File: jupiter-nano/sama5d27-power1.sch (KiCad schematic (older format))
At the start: 1 part, among them U1 ATSAMA5D27C-LD1G-CU

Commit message: WIP – power3 done
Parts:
- removed unit 8 of U1
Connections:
- net labels added: GND, VDDBU, VDDCORE, VDDIODDR, VDDIOP0, VDD_1V2, VDD_1V8
- wire segments 0 -> 128
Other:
- note added: "Power Links"
- moved on the sheet: U1F, U1G, U1I

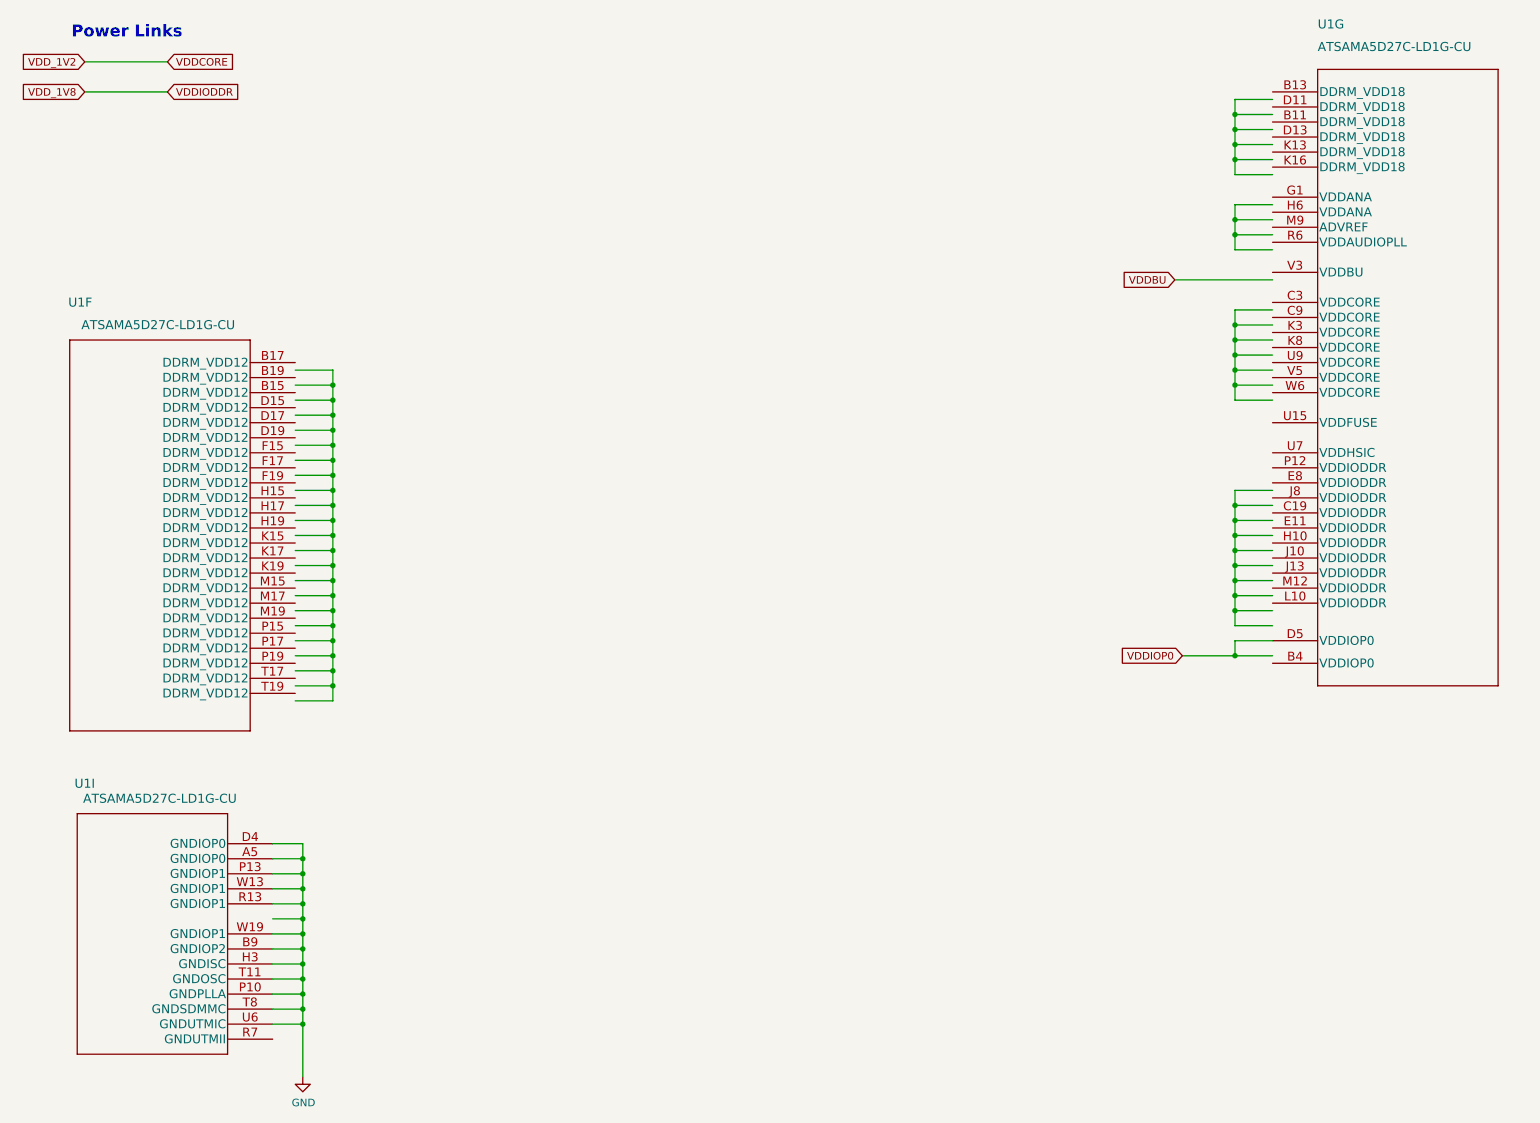
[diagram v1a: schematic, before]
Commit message: added compoent numbers for power
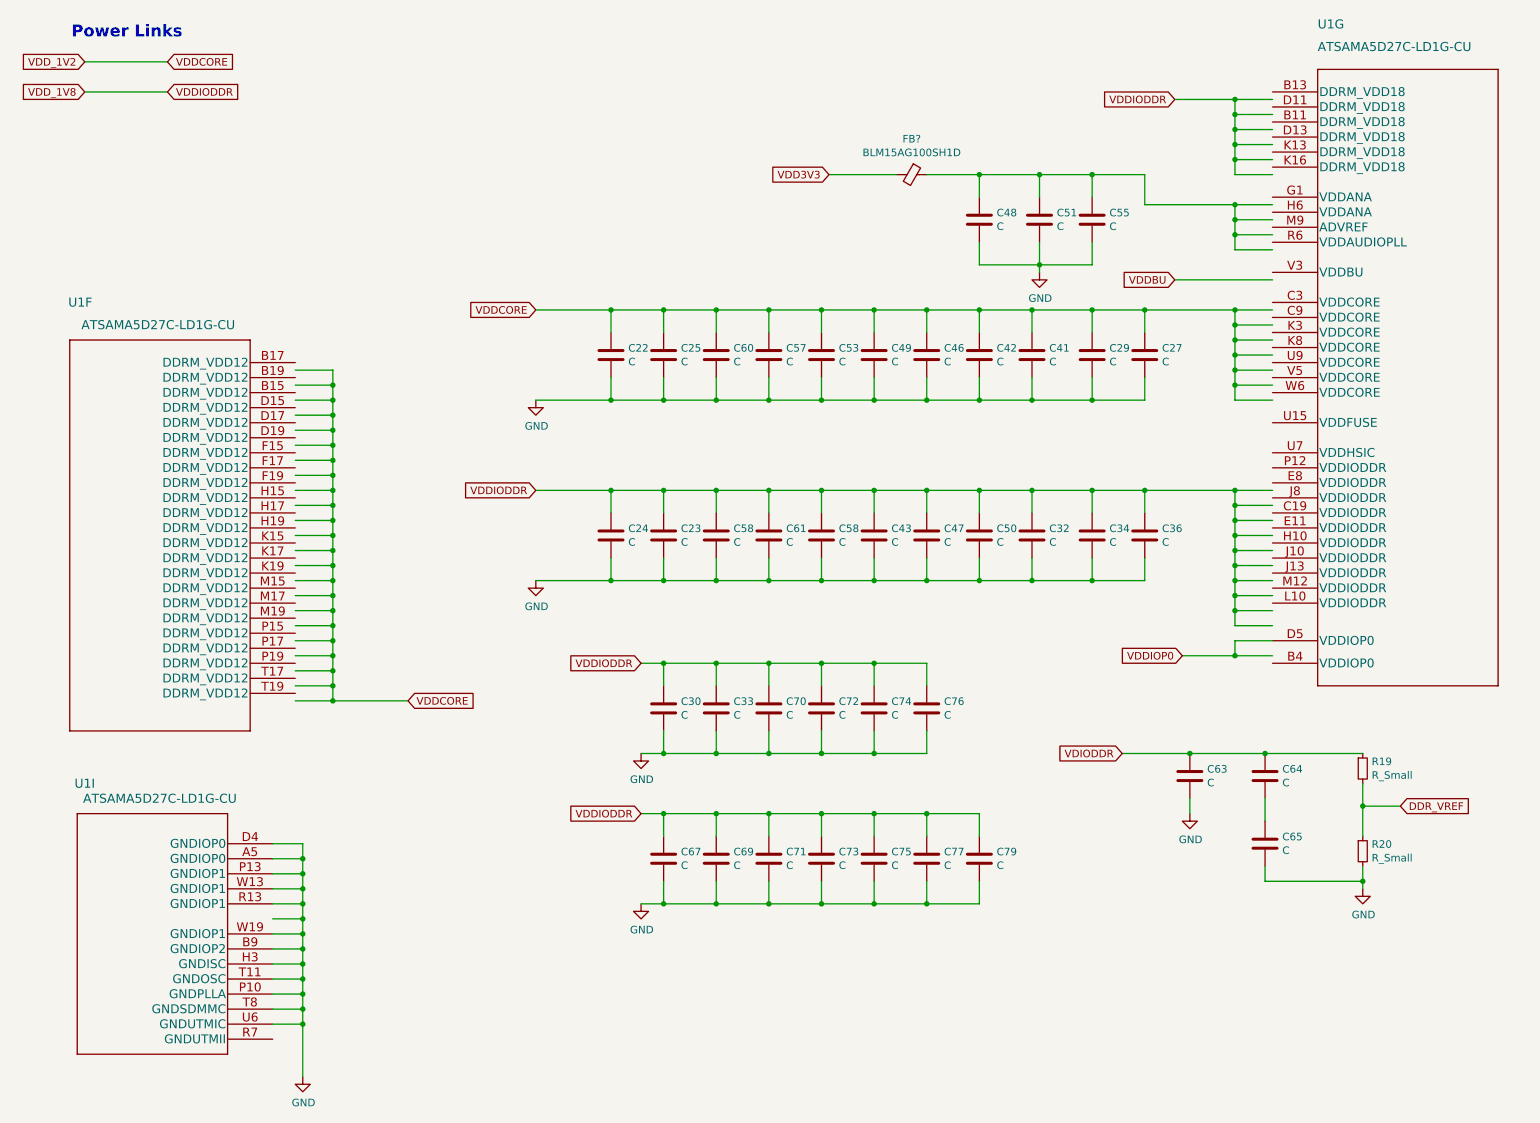
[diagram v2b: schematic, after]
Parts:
- added C22, C23, C24, C25, C27, C29, C30, C32, C33, C34, C36, C41, C42, C43, C46, C47, C48, C49, C50, C51, C53, C55, C57, C58 (x2), C60, C61, C63, C64, C65, C67, C69, C70, C71, C72, C73, C74, C75, C76, C77, C79: C, symbol Device:C
- added FB?: BLM15AG100SH1D, Capacitor_SMD:C_0402_1005Metric, symbol Device:Ferrite_Bead_Small
- added R19, R20: R_Small, symbol Device:R_Small
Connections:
- net labels added: DDR_VREF, VDD3V3, VDIODDR
- wire segments 128 -> 300

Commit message: values for power capacitors
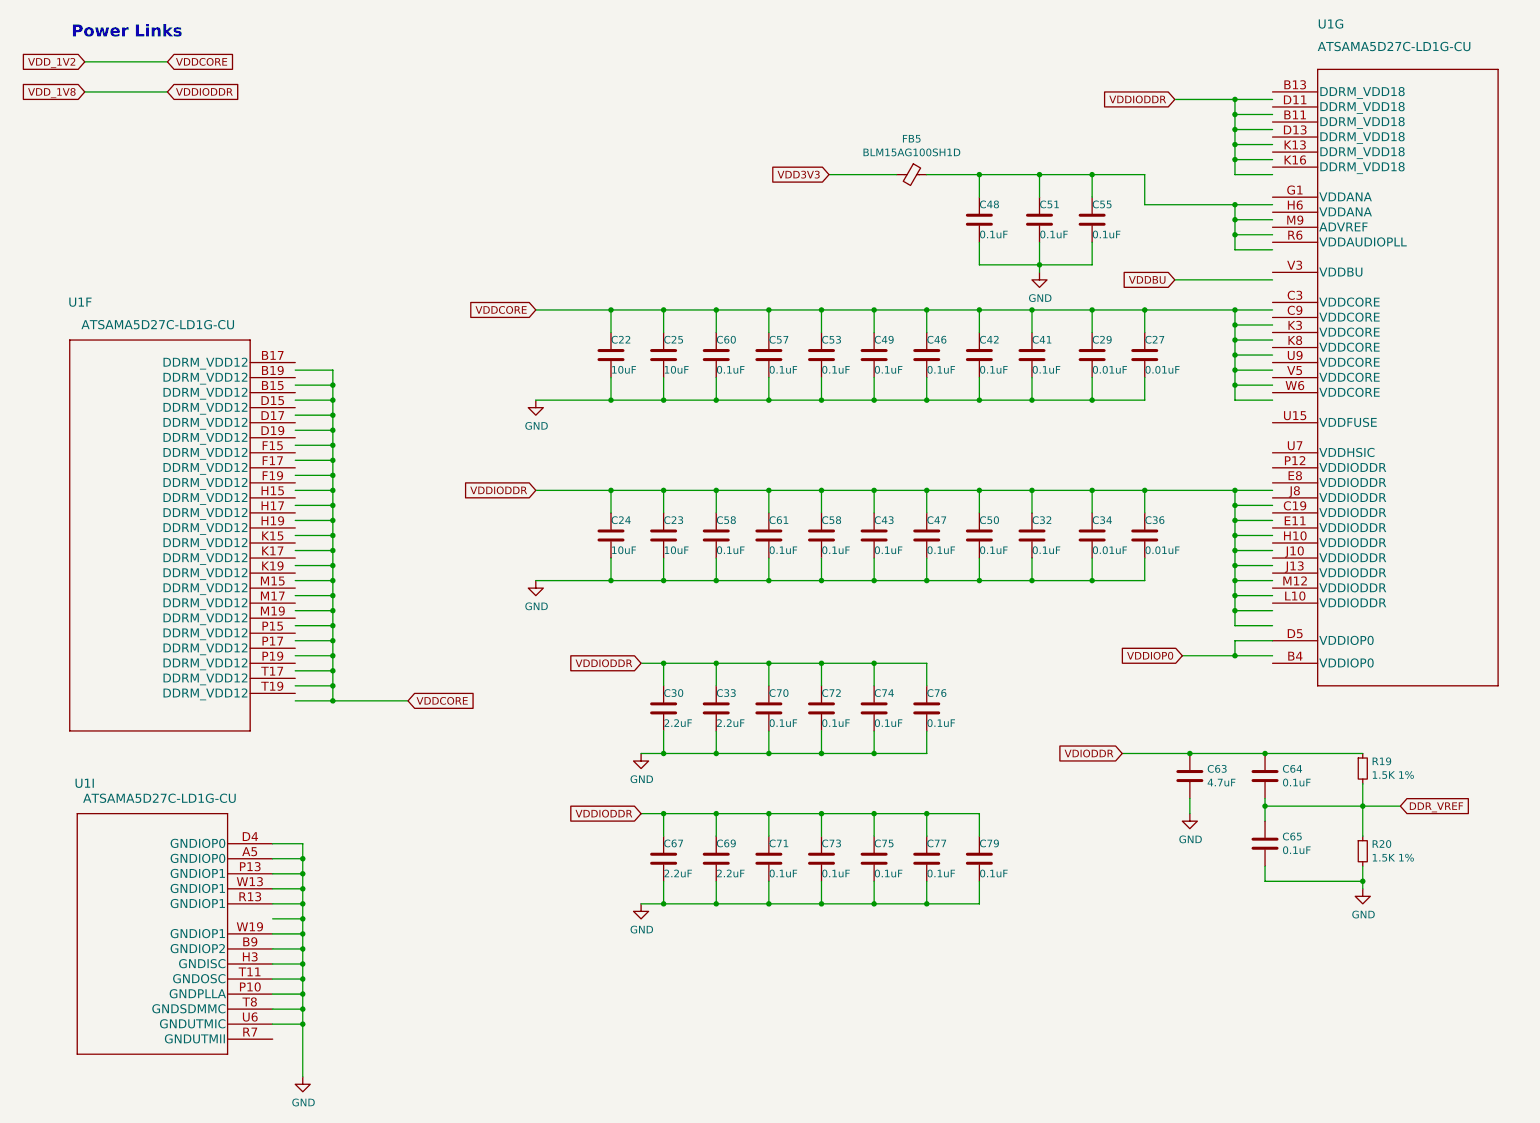
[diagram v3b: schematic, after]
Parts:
- C22, C23, C24, C25: value C -> 10uF
- C27, C29, C34, C36: value C -> 0.01uF
- C30, C33, C67, C69: value C -> 2.2uF
- C32, C41, C42, C43, C46, C47, C48, C49, C50, C51, C53, C55, C57, C58, C60, C61, C64, C65, C70, C71, C72, C73, C74, C75, C76, C77, C79: value C -> 0.1uF
- C63: value C -> 4.7uF
- R19, R20: value R_Small -> 1.5K 1%
- gave numbers to parts that had none: 1
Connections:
- wire segments 300 -> 302

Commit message: WIP, power done
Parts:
- added C40, C59, C62: 0.1uF, symbol Device:C
- added FB?: BLM15AG100SH1D, Capacitor_SMD:C_0402_1005Metric, symbol Device:Ferrite_Bead_Small
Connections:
- net labels added: VDDAUDIOPLL, VDDFUSE
- wire segments 302 -> 316
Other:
- moved on the sheet: C30, C33, C48, C51, C55, C63, C64, C65, C67, C69, C70, C71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

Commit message: WIP clocking done
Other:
- moved on the sheet: U1F, U1G
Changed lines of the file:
@@
 L ATSAMA5D27C-LD1G:ATSAMA5D27C-LD1G-CU U1
 U 6 1 5F54ECB9
-P 2300 2850
-F 0 "U1" H 3650 3300 60  0000 L CNN
-F 1 "ATSAMA5D27C-LD1G-CU" H 2700 3150 60  0000 L CNN
-F 2 "TFBGA361_16X16_MCH" H 3500 3190 60  0001 C CNN
-F 3 "" H 2300 2850 60  0000 C CNN
-	6    2300 2850
+P 2300 2900
+F 0 "U1" H 3650 3350 60  0000 L CNN
+F 1 "ATSAMA5D27C-LD1G-CU" H 2700 3200 60  0000 L CNN
+F 2 "TFBGA361_16X16_MCH" H 3500 3240 60  0001 C CNN
+F 3 "" H 2300 2900 60  0000 C CNN
+	6    2300 2900
 	-1   0    0    -1
 $EndComp
@@
 L ATSAMA5D27C-LD1G:ATSAMA5D27C-LD1G-CU U1
 U 7 1 5F56427F
-P 8800 1050
-F 0 "U1" H 9100 1550 60  0000 L CNN
-F 1 "ATSAMA5D27C-LD1G-CU" H 9100 1400 60  0000 L CNN
-F 2 "TFBGA361_16X16_MCH" H 10000 1390 60  0001 C CNN
-F 3 "" H 8800 1050 60  0000 C CNN
-	7    8800 1050
+P 8800 1100
+F 0 "U1" H 9100 1600 60  0000 L CNN
+F 1 "ATSAMA5D27C-LD1G-CU" H 9100 1450 60  0000 L CNN
+F 2 "TFBGA361_16X16_MCH" H 10000 1440 60  0001 C CNN
+F 3 "" H 8800 1100 60  0000 C CNN
+	7    8800 1100
 	1    0    0    -1
 $EndComp
@@
 Connection ~ 2350 6400
 Wire Wire Line
-	2350 6400 2350 6500
-Wire Wire Line
-	2150 6500 2350 6500
-Connection ~ 2350 6500
-Wire Wire Line
-	2350 6500 2350 6600
-Wire Wire Line
 	2150 6600 2350 6600
 Connection ~ 2350 6600
@@
 Connection ~ 2350 7200
 Wire Wire Line
-	2350 7200 2350 7550
+	2350 7200 2350 7300
 Wire Wire Line
 	2300 2850 2550 2850
@@
 Wire Wire Line
 	8550 2550 8550 2650
-Wire Wire Line
-	8800 4650 8550 4650
-Wire Wire Line
-	8550 4650 8550 4750
-Wire Wire Line
-	8550 4750 8800 4750
-Wire Wire Line
-	8550 4750 8200 4750
-Connection ~ 8550 4750
-Text GLabel 8200 4750 0    50   Input ~ 0
+Text GLabel 8100 4700 0    50   Input ~ 0
 VDDIOP0
-Wire Wire Line
-	8800 4550 8550 4550
-Wire Wire Line
-	8550 4550 8550 4450
 Wire Wire Line
 	8550 3650 8800 3650
@@
 Wire Wire Line
 	8800 4350 8550 4350
-Connection ~ 8550 4350
-Wire Wire Line
-	8550 4350 8550 4250
-Wire Wire Line
-	8800 4450 8550 4450
-Connection ~ 8550 4450
-Wire Wire Line
-	8550 4450 8550 4350
 Wire Wire Line
 	8800 1550 8550 1550
@@
 Wire Wire Line
 	8500 6100 8350 6100
+Wire Wire Line
+	2350 6400 2350 6600
+Wire Wire Line
+	2150 7300 2350 7300
+Connection ~ 2350 7300
+Wire Wire Line
+	2350 7300 2350 7550
+Wire Wire Line
+	8800 3550 8550 3550
+Wire Wire Line
+	8550 3550 8550 3650
+Wire Wire Line
+	8100 4700 8550 4700
+Wire Wire Line
+	8550 4700 8800 4700
+Connection ~ 8550 4700
+Wire Wire Line
+	8550 4700 8550 4850
+Wire Wire Line
+	8550 4850 8800 4850
+Wire Wire Line
+	8800 4450 8550 4450
+Wire Wire Line
+	8550 4250 8550 4350
+Connection ~ 8550 4350
+Wire Wire Line
+	8550 4350 8550 4450
 $EndSCHEMATC

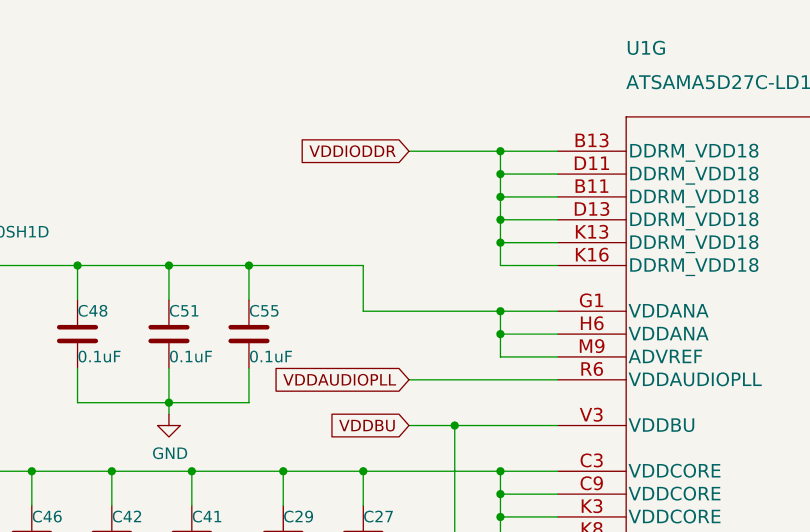
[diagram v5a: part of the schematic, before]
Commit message: WIP, connectors almost done
- still to do:
  - JTAG signals on PIO pins
  - USB-UART bridge
  - extra PIO on the header pins
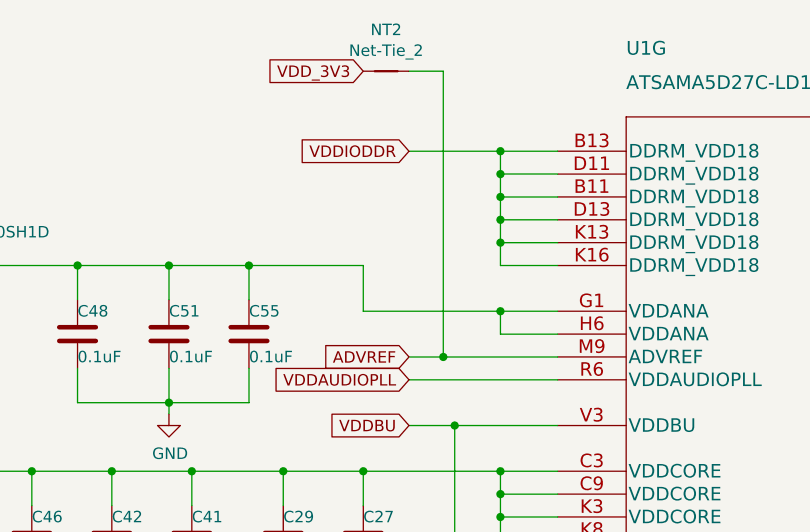
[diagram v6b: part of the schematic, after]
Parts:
- added NT2: Net-Tie_2, symbol Device:Net-Tie_2
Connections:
- net at C48.1, C51.1, C55.1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: no longer U1.M9 (ADVREF)
- new net ADVREF: NT2.2, U1.M9 (ADVREF)
- new net VDD_3V3: NT2.1
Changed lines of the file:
@@
 	8150 2050 8800 2050
 Wire Wire Line
-	8800 1950 8550 1950
+	8800 1950 8300 1950
 Wire Wire Line
 	8800 1850 8550 1850
-Connection ~ 8550 1850
-Wire Wire Line
-	8550 1850 8550 1950
 $Comp
 L Device:C C27
@@
 Wire Wire Line
 	8550 4350 8550 4450
+Text GLabel 8150 1950 0    50   Input ~ 0
+ADVREF
+Wire Wire Line
+	8300 1950 8300 700
+Wire Wire Line
+	8300 700  8150 700
+Connection ~ 8300 1950
+Wire Wire Line
+	8300 1950 8150 1950
+$Comp
+L Device:Net-Tie_2 NT2
+U 1 1 60133280
+P 8050 700
+F 0 "NT2" H 8050 881 50  0000 C CNN
+F 1 "Net-Tie_2" H 8050 790 50  0000 C CNN
+F 2 "" H 8050 700 50  0001 C CNN
+F 3 "~" H 8050 700 50  0001 C CNN
+	1    8050 700
+	1    0    0    -1
+$EndComp
+Text GLabel 7950 700  0    50   Input ~ 0
+VDD_3V3
 $EndSCHEMATC

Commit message: cleanup
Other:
- moved on the sheet: C40, FB?
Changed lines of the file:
@@
 L Device:Ferrite_Bead_Small FB?
 U 1 1 5F91D238
-P 4500 3450
+P 4350 3450
 AR Path="/5F395E67/5F91D238" Ref="FB?"  Part="1"
 AR Path="/5FD740BF/5F91D238" Ref="FB?"  Part="1"
-F 0 "FB?" V 4263 3450 50  0000 C CNN
-F 1 "BLM15AG100SH1D" V 4354 3450 50  0000 C CNN
-F 2 "Capacitor_SMD:C_0402_1005Metric" V 4430 3450 50  0001 C CNN
-F 3 "~" H 4500 3450 50  0001 C CNN
-	1    4500 3450
+F 0 "FB?" V 4113 3450 50  0000 C CNN
+F 1 "BLM15AG100SH1D" V 4204 3450 50  0000 C CNN
+F 2 "Capacitor_SMD:C_0402_1005Metric" V 4280 3450 50  0001 C CNN
+F 3 "~" H 4350 3450 50  0001 C CNN
+	1    4350 3450
 	0    1    1    0
 $EndComp
 Wire Wire Line
-	4400 3450 3900 3450
+	4250 3450 3900 3450
 Wire Wire Line
-	4600 3450 5950 3450
-Connection ~ 5950 3450
-Wire Wire Line
-	5950 3450 8800 3450
-Wire Wire Line
-	5800 3050 5950 3050
-Connection ~ 5950 3050
-Wire Wire Line
-	5950 3050 6150 3050
-Wire Wire Line
-	5950 3150 5950 3050
+	4450 3450 5100 3450
 $Comp
 L Device:C C40
 U 1 1 5F9EE154
-P 5950 3300
-F 0 "C40" H 5950 3400 50  0000 L CNN
-F 1 "0.1uF" H 5950 3200 50  0000 L CNN
-F 2 "" H 5988 3150 50  0001 C CNN
-F 3 "~" H 5950 3300 50  0001 C CNN
-	1    5950 3300
+P 5100 3300
+F 0 "C40" H 5100 3400 50  0000 L CNN
+F 1 "0.1uF" H 5100 3200 50  0000 L CNN
+F 2 "" H 5138 3150 50  0001 C CNN
+F 3 "~" H 5100 3300 50  0001 C CNN
+	1    5100 3300
 	1    0    0    -1
 $EndComp
@@
 Text GLabel 7950 700  0    50   Input ~ 0
 VDD_3V3
+Connection ~ 5100 3450
+Wire Wire Line
+	5800 3050 6150 3050
+Wire Wire Line
+	5100 3450 8800 3450
+Wire Wire Line
+	5100 3150 4900 3150
+Wire Wire Line
+	4900 3150 4900 3200
+$Comp
+L power:GND #PWR?
+U 1 1 602286E4
+P 4900 3200
+F 0 "#PWR?" H 4900 2950 50  0001 C CNN
+F 1 "GND" H 4905 3027 50  0000 C CNN
+F 2 "" H 4900 3200 50  0001 C CNN
+F 3 "" H 4900 3200 50  0001 C CNN
+	1    4900 3200
+	1    0    0    -1
+$EndComp
 $EndSCHEMATC
